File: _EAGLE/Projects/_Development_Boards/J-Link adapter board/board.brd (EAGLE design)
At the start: 40 x 60 mm, 11 parts, among them J1 PROG-HEADER_2X3_SHROUDED, J10 PROG-HEADER_2X5_1.27MM-PTH+SMD, J2 PROG-HEADER_2X5_2.00MM-SHROUD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, J3 PROG-HEADER_2X5_SHROUDED, J4 PROG-HEADER_2X7_SHROUDED, J5 PROG-HEADER_2X10_RIGHT-ANGLE, J6 PROG-HEADER_2X10_SHROUDED, J7 PROG-HEADER_2X10_2.00MM-SHROU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, J8 CONN-1X4, J9 CONN-1X6

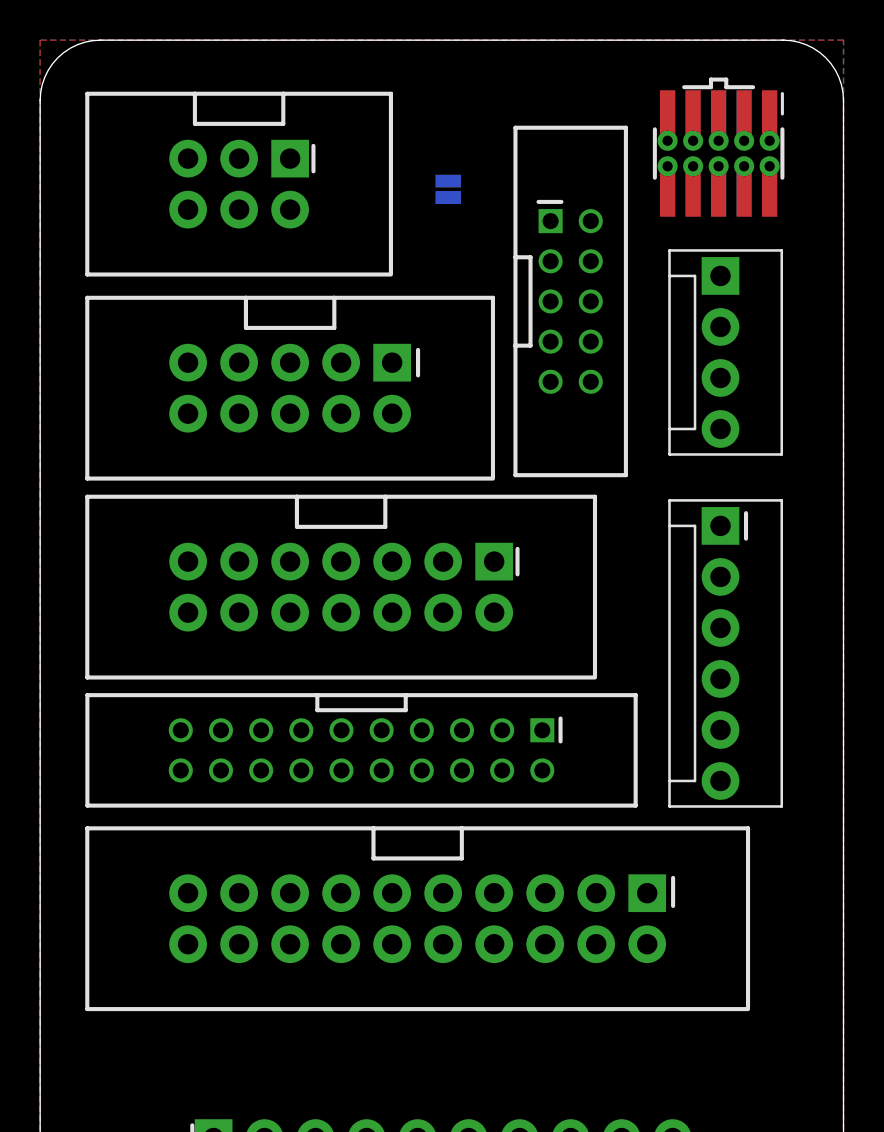
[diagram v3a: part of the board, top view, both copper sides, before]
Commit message: PCB: JTAG adapter board update
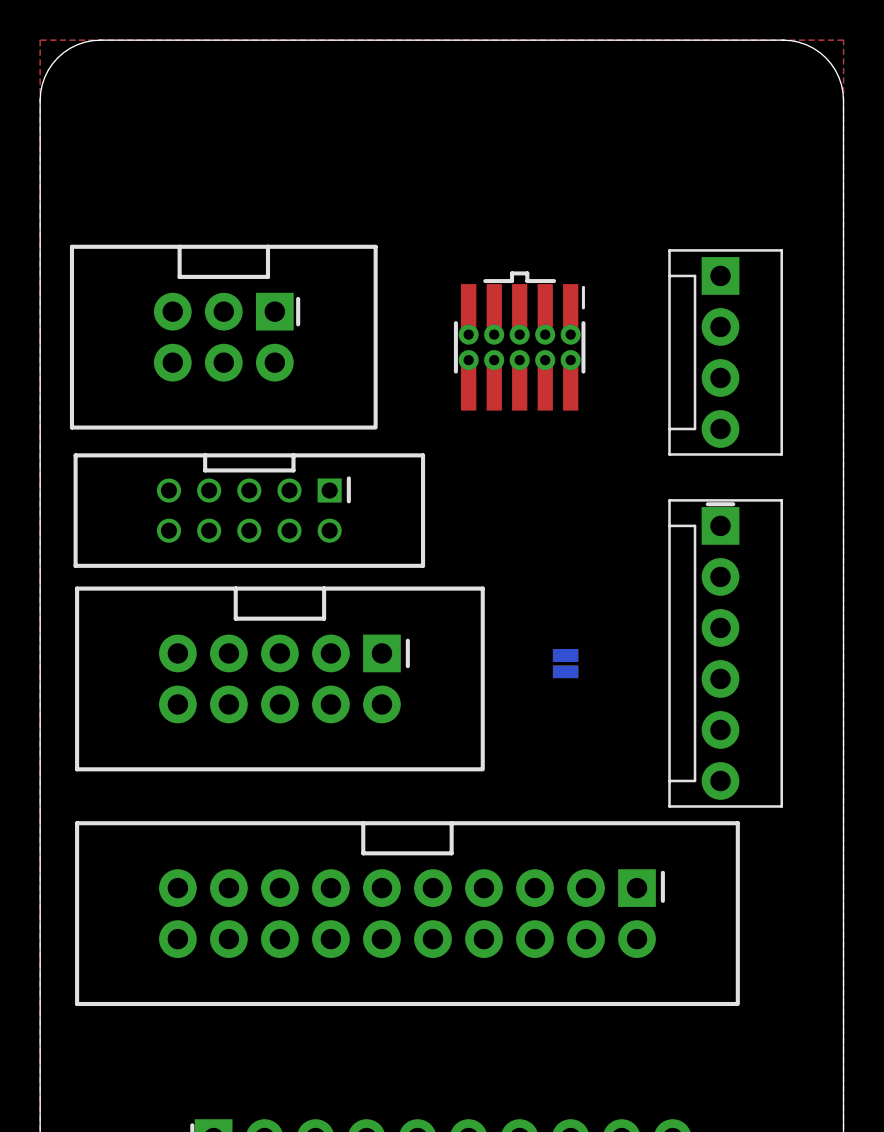
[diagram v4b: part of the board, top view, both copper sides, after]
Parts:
- removed J4: PROG-HEADER_2X7_SHROUDED, angrypig7-Connectors-Programming:2X7-2.54MM-SHROUDED
- removed J7: PROG-HEADER_2X10_2.00MM-SHROUDED, angrypig7-Connectors-Programming:2X10-2.00MM-SHROUDED
- moved JP1 24.3 mm to (26.2, 29.0)
- moved J2 19.1 mm to (10.4, 36.6), turned to 270 degrees
- moved J3 14.5 mm to (11.9, 28.2)
- moved J10 13.8 mm to (23.9, 44.7)
- moved J1 7.66 mm to (9.14, 45.2)
- moved J6 0.57 mm to (18.3, 16.5)
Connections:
- removed net (VCC): J5.2, J6.2, J7.2
- removed net /JEN: J4.1
- removed net /RST: J4.8
- removed net /TERR: J4.14
- removed net 4: J4.4
- removed net TRST: J4.2, J5.3, J6.3, J7.3
- removed net TSTAT: J4.6
- new net 2: J5.2, J6.2
- new net N$2: J10.19, J10.9
- new net NTRST: J5.3, J6.3
- net GND: now also J8.1, J9.3; no longer J10.15, J10.19, J10.5, J10.9, J2.5, J2.9, J3.5, J3.9, J4.10, J4.12, J4.3, J7.10, J7.12, J7.14, J7.16, J7.18, J7.20, J7.4, J7.6, J7.8, J8.4, J9.1
- net RST: no longer J7.15
- net RTCK: no longer J7.11
- net TCK: now also J8.2, J9.2; no longer J4.11, J7.9, J8.3, J9.3
- net TDI: no longer J4.5, J7.5
- net TDO: now also J9.6; no longer J4.13, J7.13, J9.4
- net TMS: now also J8.3, J9.4; no longer J4.9, J7.7, J8.2, J9.2
- net VCC: now also J8.4, J9.1; no longer J4.7, J7.1, J8.1, J9.6
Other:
- board text added: "SWCLK"
- board text added: "SWDIO"
- board text added: "SWO"
- board text removed: "TRST"
